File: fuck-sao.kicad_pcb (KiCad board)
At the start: 2 copper layers, 75 x 75 mm, 32 parts, among them J1 Conn_01x03_Pin, J2 Conn_02x03_Odd_Even, SW1 SW_Push, U1 ATtiny416-M

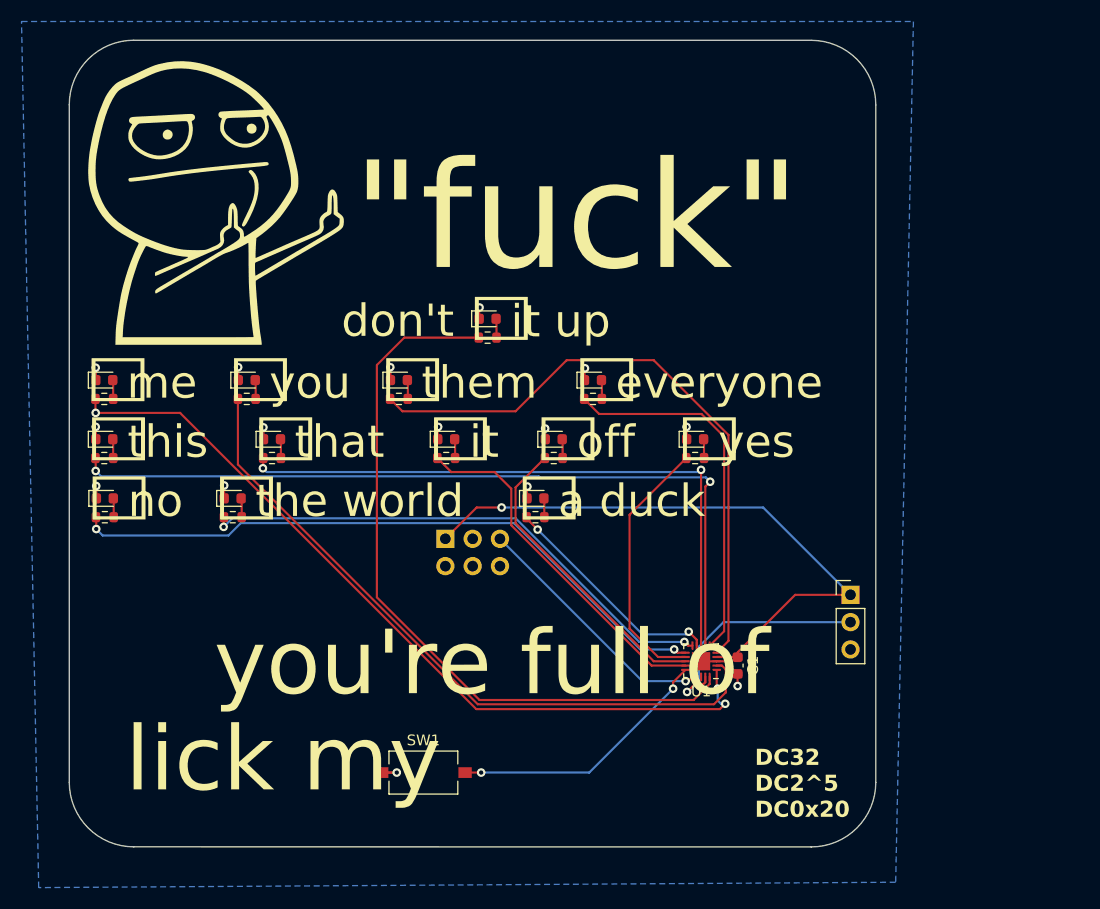
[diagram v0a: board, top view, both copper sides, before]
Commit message: new touch program and new board desigh
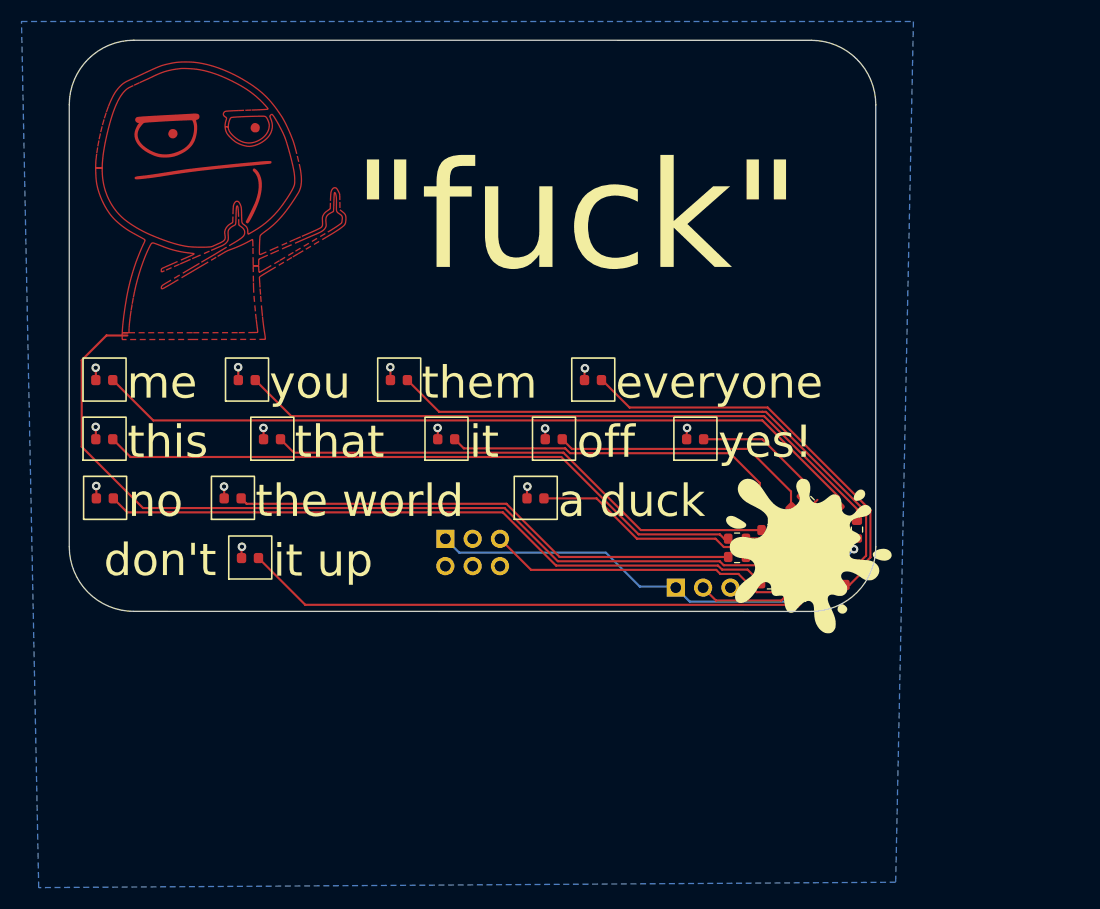
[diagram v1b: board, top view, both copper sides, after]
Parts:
- removed SW1: SW_Push, Button_Switch_SMD:SW_Tactile_SPST_NO_Straight_CK_PTS636Sx25SMTRLFS
- added R14: 1K Ohm, Resistor_SMD:R_0603_1608Metric, F.Cu at (128.9, 91.2)
- D1, D10, D11, D12, D13, D2, D3, D4, D5, D6, D7, D8, D9: footprint LED_SMD:LED_0603_1608Metric -> ws2812b-1010:LED_0603_1608Metric_large_ss
- moved R2 68.6 mm to (134.8, 86.0), turned to 45 degrees
- moved G*** 63.9 mm to (132.1, 89.9)
- moved R11 62.2 mm to (128.9, 92.7), turned to 180 degrees
- moved R6 59.3 mm to (125.8, 88.5), turned to 180 degrees
- moved R3 58.0 mm to (137.0, 87.7), turned to 90 degrees
- moved R12 47.0 mm to (125.8, 90.2), turned to 180 degrees
- moved R7 46.8 mm to (128.9, 87.7), turned to 180 degrees
- moved R4 44.5 mm to (136.2, 90.9)
- moved R1 37.9 mm to (132.0, 93.8), turned to -135 degrees
- moved D1 31.4 mm to (80.5, 90.3)
- moved R8 30.1 mm to (128.6, 85.4), turned to 135 degrees
- moved R5 28.5 mm to (135.1, 92.8)
- moved R9 23.2 mm to (131.4, 86.2), turned to 135 degrees
- moved R13 22.0 mm to (128.9, 89.2), turned to 180 degrees
- moved J1 16.3 mm to (120.2, 93.0), turned to 90 degrees
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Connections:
- R10 pad 1: Net-(U1-PB2) -> Net-(U1-PA6)
- R11 pad 1: Net-(U1-PB3) -> Net-(U1-PC0)
- R12 pad 1: Net-(U1-PB4) -> Net-(U1-PB1)
- R13 pad 1: Net-(U1-PB5) -> Net-(U1-PB2)
- R2 pad 1: Net-(U1-PA2) -> Net-(U1-PA5)
- R3 pad 1: Net-(U1-PA3) -> Net-(U1-PA4)
- R4 pad 1: Net-(U1-PA4) -> Net-(U1-PA3)
- R5 pad 1: Net-(U1-PA5) -> Net-(U1-PA2)
- R6 pad 1: Net-(U1-PA6) -> Net-(U1-PB3)
- R7 pad 1: Net-(U1-PA7) -> Net-(U1-PB4)
- R8 pad 1: Net-(U1-PB0) -> Net-(U1-PB5)
- R9 pad 1: Net-(U1-PB1) -> Net-(U1-PA7)
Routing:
- net unconnected-(R14-Pad2): track 0.00 -> 81.1 mm
- net Net-(U1-PA2): track 75.2 -> 2.16 mm, vias 3 -> 0
- net Net-(D2-A): track 1.77 -> 72.9 mm
- net Net-(U1-PA6): track 74.2 -> 3.76 mm, vias 2 -> 0
- net Net-(U1-PA1): track 68.3 -> 2.13 mm
- net Net-(U1-PA3): track 64.3 -> 1.60 mm
- net Net-(D11-A): track 1.77 -> 63.5 mm
- net Net-(D3-A): track 1.77 -> 62.1 mm
- net Net-(D6-A): track 1.77 -> 61.1 mm
- net Net-(U1-PA4): track 57.5 -> 0.28 mm
- net Net-(U1-PB3): track 61.6 -> 4.74 mm, vias 2 -> 0
- net Net-(U1-PA7): track 58.3 -> 1.93 mm, vias 2 -> 0
- net Net-(D4-A): track 1.77 -> 53.0 mm
- net Net-(D1-A): track 1.77 -> 52.0 mm
- net Net-(U1-PB4): track 49.8 -> 2.34 mm, vias 2 -> 0
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- added copper zone on F.Cu, net unconnected-(R14-Pad2)
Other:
- board size 75 x 75 mm -> 75 x 53.1 mm
- board text added: "Touch the dude on the front to change selection"
- board text added: "yes!"
- board text removed: "lick my"
- board text removed: "yes"
- board text removed: "you're full of"
- board text removed: "☐"

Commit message: PCB rules addressed
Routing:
- net Net-(U1-PA4): track 0.28 -> 3.28 mm
- net Net-(U1-PA6): track 3.76 -> 2.87 mm
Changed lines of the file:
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@@
   (segment (start 71.5505 77.5005) (end 128.2005 77.5005) (width 0.2) (layer "F.Cu") (net 4))
   (segment (start 67.8 73.75) (end 71.5505 77.5005) (width 0.2) (layer "F.Cu") (net 4))
-  (segment (start 67.7875 73.75) (end 67.8 73.75) (width 0.2) (layer "F.Cu") (net 4))
   (segment (start 135.333363 84.633363) (end 135.333363 85.466637) (width 0.2) (layer "F.Cu") (net 4))
-  (segment (start 67.825 73.7875) (end 67.7875 73.75) (width 0.2) (layer "F.Cu") (net 4))
   (segment (start 128.2005 77.5005) (end 135.333363 84.633363) (width 0.2) (layer "F.Cu") (net 4))
   (segment (start 137 86.825) (end 137 85.73502) (width 0.2) (layer "F.Cu") (net 5))
-  (segment (start 81.075 73.7875) (end 81.0375 73.75) (width 0.2) (layer "F.Cu") (net 5))
   (segment (start 128.365979 77.100999) (end 84.388499 77.100999) (width 0.2) (layer "F.Cu") (net 5))
   (segment (start 137 85.73502) (end 128.365979 77.100999) (width 0.2) (layer "F.Cu") (net 5))
@@
   (segment (start 137.85 90.075) (end 137.85 86.02004) (width 0.2) (layer "F.Cu") (net 6))
   (segment (start 98.138499 76.700999) (end 95.1875 73.75) (width 0.2) (layer "F.Cu") (net 6))
-  (segment (start 95.225 73.7875) (end 95.1875 73.75) (width 0.2) (layer "F.Cu") (net 6))
   (segment (start 128.531458 76.701498) (end 128.202204 76.701498) (width 0.2) (layer "F.Cu") (net 6))
   (segment (start 137.725 91.382107) (end 137.725 90.765686) (width 0.2) (layer "F.Cu") (net 7))
@@
   (segment (start 104.395938 85.250998) (end 109.34494 90.2) (width 0.2) (layer "F.Cu") (net 14))
   (segment (start 80.225998 85.250998) (end 104.395938 85.250998) (width 0.2) (layer "F.Cu") (net 14))
-  (segment (start 107.925 84.7875) (end 107.8875 84.75) (width 0.2) (layer "F.Cu") (net 15))
-  (segment (start 124.617893 89.275) (end 123.842893 88.5) (width 0.2) (layer "F.Cu") (net 15))
   (segment (start 123.842893 88.5) (end 116.534314 88.5) (width 0.2) (layer "F.Cu") (net 15))
+  (segment (start 128.125 89.25) (end 127.5 89.25) (width 0.2) (layer "F.Cu") (net 15))
+  (segment (start 127.4 89.35) (end 124.692893 89.35) (width 0.2) (layer "F.Cu") (net 15))
   (segment (start 112.784314 84.75) (end 107.8875 84.75) (width 0.2) (layer "F.Cu") (net 15))
-  (segment (start 127.107107 89.25) (end 127.082107 89.275) (width 0.2) (layer "F.Cu") (net 15))
-  (segment (start 128.125 89.25) (end 127.107107 89.25) (width 0.2) (layer "F.Cu") (net 15))
-  (segment (start 127.082107 89.275) (end 124.617893 89.275) (width 0.2) (layer "F.Cu") (net 15))
+  (segment (start 127.5 89.25) (end 127.4 89.35) (width 0.2) (layer "F.Cu") (net 15))
   (segment (start 116.534314 88.5) (end 112.784314 84.75) (width 0.2) (layer "F.Cu") (net 15))
+  (segment (start 124.692893 89.35) (end 123.842893 88.5) (width 0.2) (layer "F.Cu") (net 15))
   (segment (start 122.69 93.05) (end 123.89 94.25) (width 0.2) (layer "F.Cu") (net 16))
   (segment (start 132.95 91.894975) (end 132.95 91.4) (width 0.2) (layer "F.Cu") (net 16))
@@
   (segment (start 133.35 92.45) (end 132.583363 93.216637) (width 0.2) (layer "F.Cu") (net 25))
   (segment (start 131.1 91.275) (end 129.725 92.65) (width 0.2) (layer "F.Cu") (net 26))
-  (segment (start 129.825 92.55) (end 129.725 92.65) (width 0.2) (layer "F.Cu") (net 26))
-  (segment (start 129.825 92.375) (end 129.825 92.55) (width 0.2) (layer "F.Cu") (net 26))
   (segment (start 131.1 90.75) (end 131.1 91.275) (width 0.2) (layer "F.Cu") (net 26))
   (segment (start 130.440045 89.95) (end 130.190045 90.2) (width 0.2) (layer "F.Cu") (net 27))
@@
   (segment (start 133.35 87.45) (end 134.166637 86.633363) (width 0.2) (layer "F.Cu") (net 29))
   (segment (start 133.35 88.5) (end 133.35 87.45) (width 0.2) (layer "F.Cu") (net 29))
-  (segment (start 136.8 88.275) (end 137 88.475) (width 0.2) (layer "F.Cu") (net 30))
+  (segment (start 136.9 88.575) (end 137 88.475) (width 0.2) (layer "F.Cu") (net 30))
+  (segment (start 134.575 88.575) (end 136.9 88.575) (width 0.2) (layer "F.Cu") (net 30))
+  (segment (start 134 89.15) (end 134.575 88.575) (width 0.2) (layer "F.Cu") (net 30))
   (segment (start 134.825 90.35) (end 135.375 90.9) (width 0.2) (layer "F.Cu") (net 31))
   (segment (start 134 90.35) (end 134.825 90.35) (width 0.2) (layer "F.Cu") (net 31))
@@
   (segment (start 132.55 88.5) (end 132.55 87.3) (width 0.2) (layer "F.Cu") (net 36))
   (segment (start 132.95 88.5) (end 132.95 86.45) (width 0.2) (layer "F.Cu") (net 37))
-  (segment (start 133.083363 85.133363) (end 133.083363 85.683363) (width 0.2) (layer "F.Cu") (net 37))
   (segment (start 132.95 86.45) (end 133.083363 86.316637) (width 0.2) (layer "F.Cu") (net 37))
-  (segment (start 133.325 84.891726) (end 133.083363 85.133363) (width 0.2) (layer "F.Cu") (net 37))
   (segment (start 133.083363 86.316637) (end 133.083363 85.683363) (width 0.2) (layer "F.Cu") (net 37))
   (zone (net 24) (net_name "unconnected-(R14-Pad2)") (layer "F.Cu") (hatch edge 0.5)
@@
     (connect_pads (clearance 0))
     (min_thickness 0.25) (filled_areas_thickness no)
-    (fill (thermal_gap 0.5) (thermal_bridge_width 0.5))
+    (fill yes (thermal_gap 0.5) (thermal_bridge_width 0.5))
     (polygon
       (pts
@@
     (connect_pads (clearance 0.5))
     (min_thickness 0.25) (filled_areas_thickness no)
-    (fill (thermal_gap 0.5) (thermal_bridge_width 0.5) (island_removal_mode 2) (island_area_min 10))
+    (fill yes (thermal_gap 0.5) (thermal_bridge_width 0.5) (island_removal_mode 2) (island_area_min 10))
     (polygon
       (pts
@@
     (connect_pads (clearance 0.5))
     (min_thickness 0.25) (filled_areas_thickness no)
-    (fill (thermal_gap 0.5) (thermal_bridge_width 0.5))
+    (fill yes (thermal_gap 0.5) (thermal_bridge_width 0.5))
     (polygon
       (pts
@@
     (connect_pads (clearance 0.5))
     (min_thickness 0.25) (filled_areas_thickness no)
-    (fill (thermal_gap 0.5) (thermal_bridge_width 0.5))
+    (fill yes (thermal_gap 0.5) (thermal_bridge_width 0.5))
     (polygon
       (pts
@@
     (connect_pads (clearance 0.5))
     (min_thickness 0.25) (filled_areas_thickness no)
-    (fill (thermal_gap 0.5) (thermal_bridge_width 0.5))
+    (fill yes (thermal_gap 0.5) (thermal_bridge_width 0.5))
     (polygon
       (pts
@@
     (connect_pads (clearance 0.5))
     (min_thickness 0.25) (filled_areas_thickness no)
-    (fill (thermal_gap 0.5) (thermal_bridge_width 0.5))
+    (fill yes (thermal_gap 0.5) (thermal_bridge_width 0.5))
     (polygon
       (pts
@@
     (connect_pads (clearance 0.5))
     (min_thickness 0.25) (filled_areas_thickness no)
-    (fill (thermal_gap 0.5) (thermal_bridge_width 0.5))
+    (fill yes (thermal_gap 0.5) (thermal_bridge_width 0.5))
     (polygon
       (pts
@@
     (connect_pads (clearance 0.5))
     (min_thickness 0.25) (filled_areas_thickness no)
-    (fill (thermal_gap 0.5) (thermal_bridge_width 0.5))
+    (fill yes (thermal_gap 0.5) (thermal_bridge_width 0.5))
     (polygon
       (pts

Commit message: media and more
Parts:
- added BT1: Battery_Cell, COIN CELL BATTERY HOLDER TBH-CR2032-M04, B.Cu at (77.7, 52.0)
- added SW1: SW_Nidec_CAS-120A1, Connector_PinHeader_2.54mm:PinHeader_1x02_P2.54mm_Vertical, F.Cu at (115.1, 93.0)
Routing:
- net Net-(BT1-+): track 0.00 -> 97.2 mm
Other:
- board text added: "Switch"
